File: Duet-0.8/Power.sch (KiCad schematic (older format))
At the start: 22 parts, among them U2 TC2117-3.3VDBTR, U3 MC7805CDTG

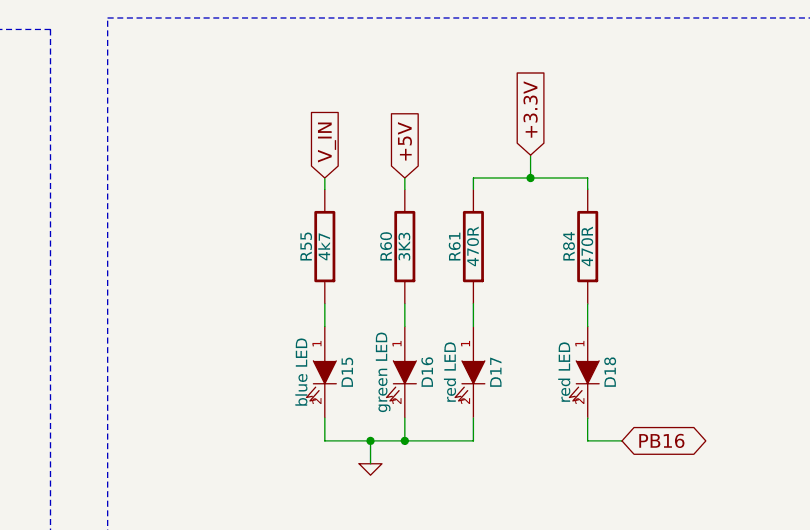
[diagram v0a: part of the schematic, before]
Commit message: USB B connector used.  Always-on fan connector added next to heater connector. Green power LED (5v) now has a bigger ballast resistor.
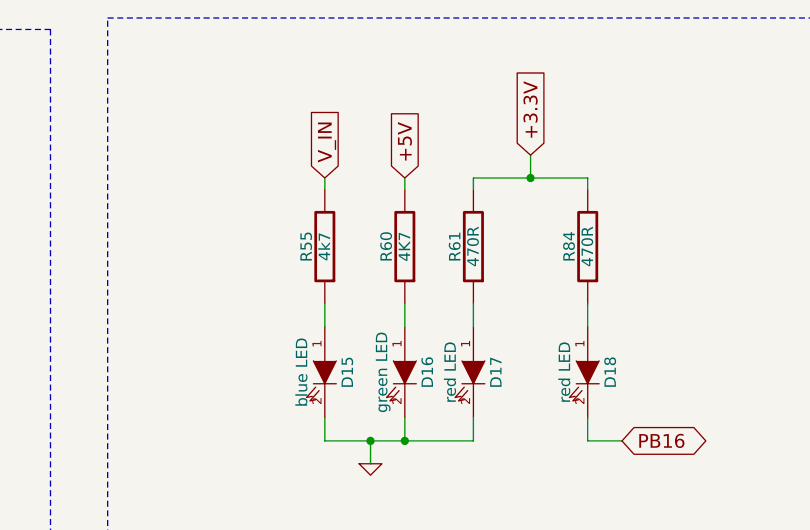
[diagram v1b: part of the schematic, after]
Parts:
- R60: value 3K3 -> 4K7
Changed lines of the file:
@@
 Sheet 3 7
 Title "Duet"
-Date "18 mar 2015"
+Date "8 jul 2015"
 Rev "0.7"
 Comp "Think3DPrint3D, RepRapPro"
@@
 P 8800 2050
 F 0 "R60" V 8880 2050 50  0000 C CNN
-F 1 "3K3" V 8800 2050 50  0000 C CNN
+F 1 "4K7" V 8800 2050 50  0000 C CNN
 F 2 "" H 8800 2050 60  0001 C CNN
 F 3 "" H 8800 2050 60  0001 C CNN

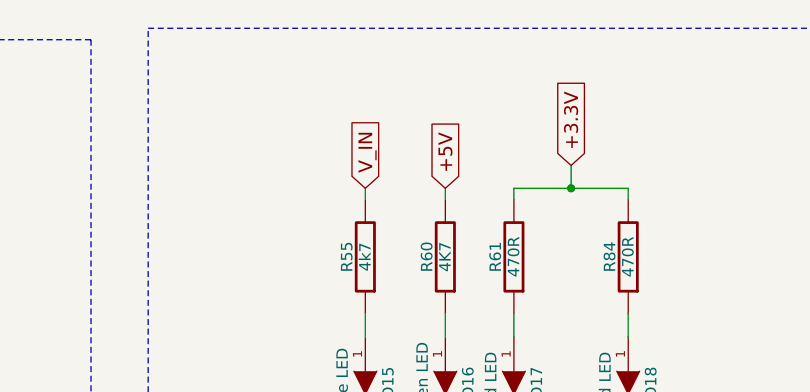
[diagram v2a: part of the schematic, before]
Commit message: Duet 0.8 power voltage test points added.  Ballast resistors on power LEDs changed to make each the same brightness (allowing for the fact that the human eye sees green as a lot brighter than blue or red).
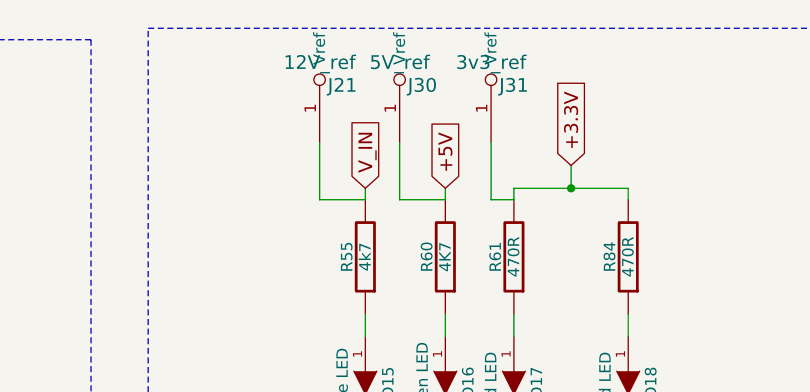
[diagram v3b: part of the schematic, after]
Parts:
- added J21: 12V_ref, ~, symbol VREF
- added J30: 5V_ref, ~, symbol VREF
- added J31: 3v3_ref, ~, symbol VREF
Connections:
- net +3.3V: now also J31.1 (Vref)
- net +5V: now also J30.1 (Vref)
- net V_IN: now also J21.1 (Vref)
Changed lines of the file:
@@
 PS_ON Control
 $Comp
-L GND #PWR030
+L GND #PWR32
 U 1 1 5220BA8F
 P 6600 5500
-F 0 "#PWR030" H 6600 5500 30  0001 C CNN
+F 0 "#PWR32" H 6600 5500 30  0001 C CNN
 F 1 "GND" H 6600 5430 30  0001 C CNN
 F 2 "" H 6600 5500 60  0001 C CNN
@@
 +5V
 $Comp
-L GND #PWR031
+L GND #PWR30
 U 1 1 50522574
 P 2000 5550
-F 0 "#PWR031" H 2000 5550 30  0001 C CNN
+F 0 "#PWR30" H 2000 5550 30  0001 C CNN
 F 1 "GND" H 2000 5480 30  0001 C CNN
 F 2 "" H 2000 5550 60  0001 C CNN
@@
 $EndComp
 $Comp
-L GND #PWR032
+L GND #PWR31
 U 1 1 50522566
 P 3200 3000
-F 0 "#PWR032" H 3200 3000 30  0001 C CNN
+F 0 "#PWR31" H 3200 3000 30  0001 C CNN
 F 1 "GND" H 3200 2930 30  0001 C CNN
 F 2 "" H 3200 3000 60  0001 C CNN
@@
 +3.3V
 $Comp
-L GND #PWR033
+L GND #PWR33
 U 1 1 54EF3E25
 P 8650 3000
-F 0 "#PWR033" H 8650 3000 30  0001 C CNN
+F 0 "#PWR33" H 8650 3000 30  0001 C CNN
 F 1 "GND" H 8650 2930 30  0001 C CNN
 F 2 "" H 8650 3000 60  0001 C CNN
@@
 Wire Wire Line
 	6550 1800 6500 1800
+$Comp
+L VREF J31
+U 1 1 559E5E20
+P 9000 1550
+F 0 "J31" H 9100 1800 60  0000 C CNN
+F 1 "3v3_ref" H 9000 1900 60  0000 C CNN
+F 2 "~" H 9000 1550 60  0000 C CNN
+F 3 "~" H 9000 1550 60  0000 C CNN
+	1    9000 1550
+	1    0    0    -1
+$EndComp
+$Comp
+L VREF J30
+U 1 1 559E5E2F
+P 8600 1550
+F 0 "J30" H 8700 1800 60  0000 C CNN
+F 1 "5V_ref" H 8600 1900 60  0000 C CNN
+F 2 "~" H 8600 1550 60  0000 C CNN
+F 3 "~" H 8600 1550 60  0000 C CNN
+	1    8600 1550
+	1    0    0    -1
+$EndComp
+$Comp
+L VREF J21
+U 1 1 559E5E3E
+P 8250 1550
+F 0 "J21" H 8350 1800 60  0000 C CNN
+F 1 "12V_ref" H 8250 1900 60  0000 C CNN
+F 2 "~" H 8250 1550 60  0000 C CNN
+F 3 "~" H 8250 1550 60  0000 C CNN
+	1    8250 1550
+	1    0    0    -1
+$EndComp
+Wire Wire Line
+	8250 1550 8250 1800
+Wire Wire Line
+	8250 1800 8450 1800
+Wire Wire Line
+	8600 1550 8600 1800
+Wire Wire Line
+	8600 1800 8800 1800
+Wire Wire Line
+	9000 1550 9000 1800
+Wire Wire Line
+	9000 1800 9100 1800
 $EndSCHEMATC
